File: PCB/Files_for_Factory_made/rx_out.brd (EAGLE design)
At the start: 93.8 x 63.8 mm, 8 parts

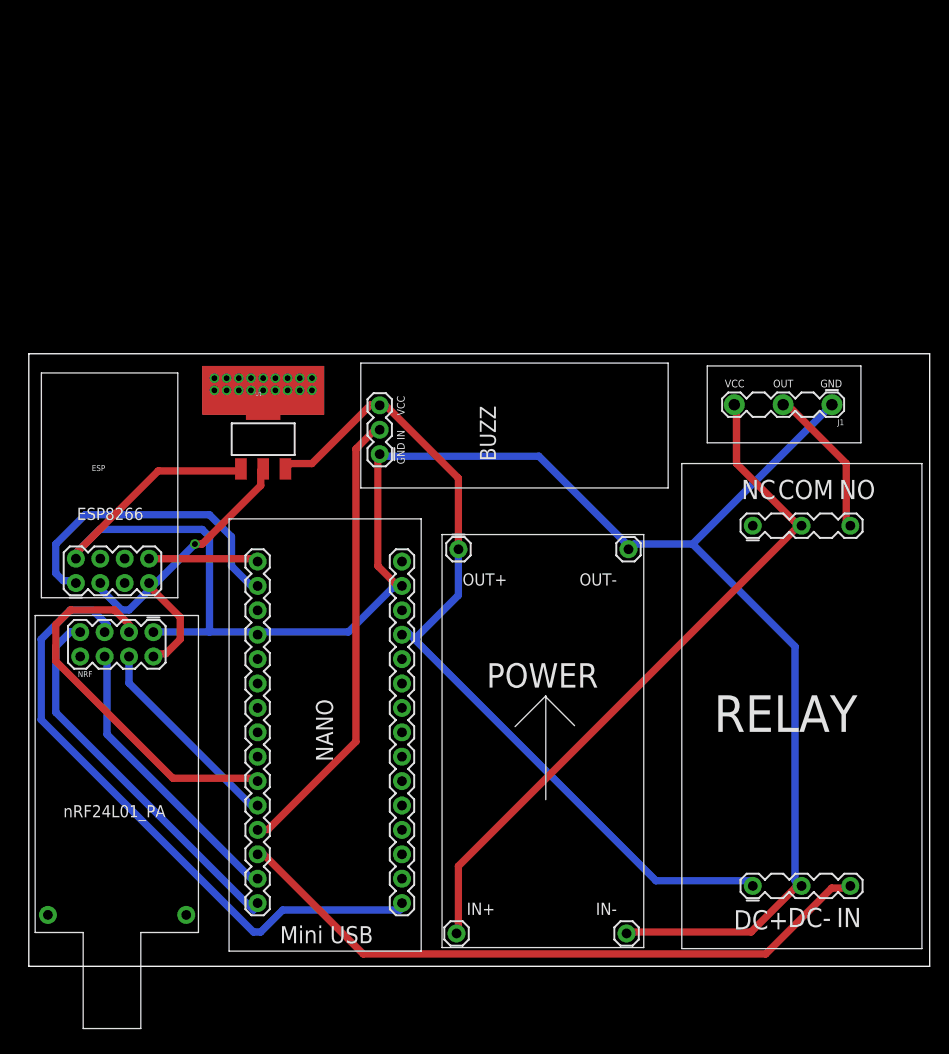
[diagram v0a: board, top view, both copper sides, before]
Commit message: pcb_out,arduino struct
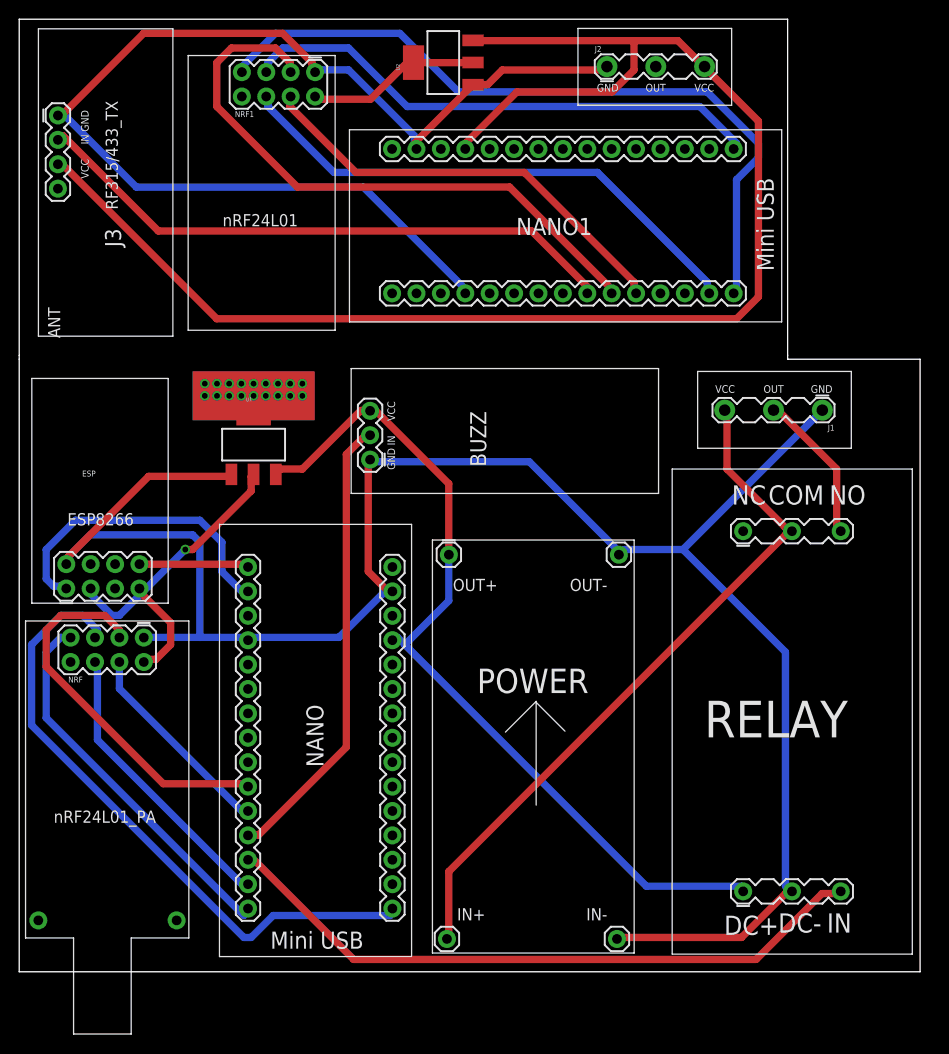
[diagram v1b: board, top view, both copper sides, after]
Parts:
- added J2: (no value), rx:OUT_HEAD_3_BIG
- added J3: (no value), rx:315MHZ_TX
- added NANO1: (no value), rx:ARDUINO_NANO
- added NRF1: (no value), rx:NRF24L01
- added U2: (no value), rx:SOT223
- moved ESP 1.15 mm to (15.5, 38.8)
- moved BUZZ 1.15 mm to (34.6, 50.2)
- moved J1 1.15 mm to (86.6, 62.9)
- moved NANO 1.15 mm to (30.8, 17.2)
- moved NRF 1.15 mm to (9.16, 19.8)
- moved POWER 1.15 mm to (54.9, 23.6)
- moved RELAY 1.15 mm to (80.3, 31.2)
- moved U1 1.15 mm to (24.4, 55.3)
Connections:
- new net +3.3V1: NRF1.2, U2.2, U2.4
- new net +5V1: J2.5, J3.5, NANO1.12, U2.3
- new net D1: NANO1.17, NRF1.6
- new net D14: NANO1.19
- new net D15: J3.3, NANO1.22
- new net D2: NANO1.20, NRF1.4
- new net D3: NANO1.1, NRF1.5
- new net D4: NANO1.21, NRF1.3
- new net D5: NANO1.16, NRF1.7
- new net D6: NANO1.18
- new net GND1: J2.1, J3.1, NANO1.14, NANO1.27, NRF1.1, U2.1
- new net NANO_RX1: NANO1.29
- new net NANO_TX1: NANO1.30
- new net OUT1: J2.3
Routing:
- net +5V1: track 0.00 -> 156.3 mm
- net GND1: track 0.00 -> 121.5 mm
- net D5: track 0.00 -> 77.5 mm
- net D4: track 0.00 -> 63.9 mm
- net D15: track 0.00 -> 62.7 mm
- net D1: track 0.00 -> 55.6 mm
- net D3: track 0.00 -> 55.2 mm
- net D2: track 0.00 -> 45.7 mm
- net +3.3V1: track 0.00 -> 18.1 mm
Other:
- board size 93.8 x 63.8 mm -> 93.8 x 99.2 mm
